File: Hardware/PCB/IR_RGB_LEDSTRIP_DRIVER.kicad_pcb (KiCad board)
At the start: 2 copper layers, 91 x 55.5 mm, 25 parts, among them J1 Barrel_Jack, J2 Conn_01x04_Female, J3 ICSP connector, Q1 IRLZ34N, Q2 IRLZ34N, Q3 IRLZ34N, SW1 SW_RESET, U1 TSOP134xx, U2 L7805, U3 ATmega328P-PU

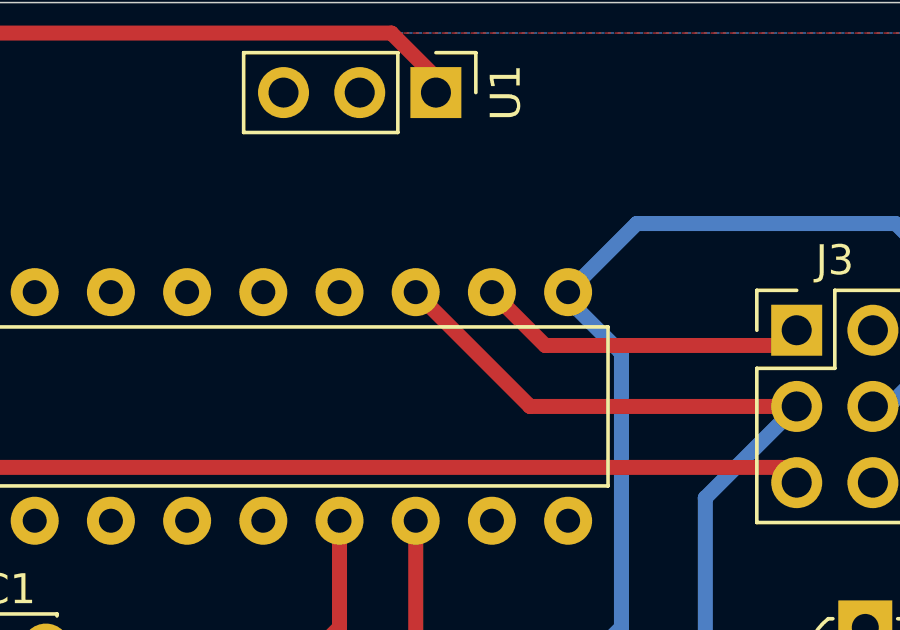
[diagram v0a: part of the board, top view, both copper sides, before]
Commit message: Fixed connection error for the ICSP port
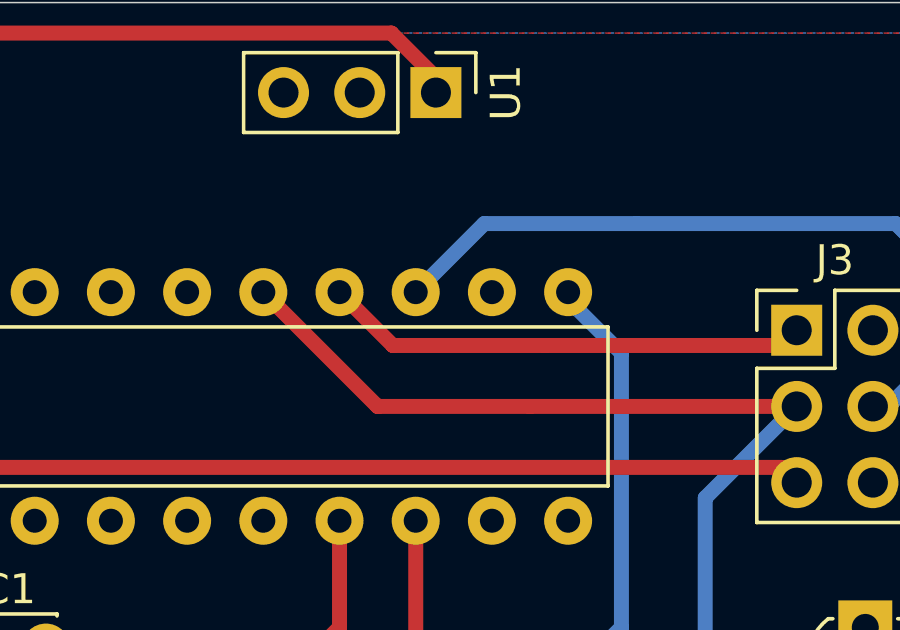
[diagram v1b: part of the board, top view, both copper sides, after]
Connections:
- J3 pad 4: GREEN_SIGNAL -> Net-(J3-Pad4)
- U3 pad 16: Net-(J3-Pad1) -> Net-(U3-Pad16)
- U3 pad 17: Net-(J3-Pad3) -> Net-(J3-Pad4)
- U3 pad 18: Net-(U3-Pad18) -> Net-(J3-Pad1)
- U3 pad 19: Net-(U3-Pad19) -> Net-(J3-Pad3)
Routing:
- net Net-(J3-Pad4): track 0.00 -> 24.7 mm
- net GREEN_SIGNAL: track 34.4 -> 14.8 mm
- net Net-(J3-Pad1): track 11.1 -> 16.2 mm
- net Net-(J3-Pad3): track 25.0 -> 30.1 mm
